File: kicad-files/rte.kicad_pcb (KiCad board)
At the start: 2 copper layers, 120.1 x 58.9 mm, 77 parts, among them J1 APU_LED_INPUT, J10 EXP_GPIO_OUTPUT, J11 OC BUFFER OUTPUT, J12 APU_POWER_SUPPLY_INPUT, J13 APU_POWER_SUPPLY_OUTPUT, J14 RS232, J15 5V_POWER_SUPPLY, J16 UART OUTPUT SELECT, J17 USB_POWER_SUPPLY, J18 EXTERNAL UART, J2 ORANGE_PI_ZERO_SERIAL_OUT, J3 ORANGE_PI_ZERO_CONN2, J4 ORANGE_PI_ZERO_SERIAL_IN, J5 ORANGE_PI_ZERO_CONN1, J6 USB_A1, J7 SPI_OUTPUT, J8 USB_A2, J9 I2C_BUS_OUTPUT, K1 HF3FA, K2 FTR-B3CA003Z, Q1 NDS351AN, Q2 NDS351AN, Q5 Si9435BDY, SW1 RESET, U1 MCP23017, U2 74LS06, U3 MAX3232, U4 74LS06, U5 TXS0104E, U6 MIC5504-1.8YM5, U7 MIC5504-3.3YM5, U8 FDC6331L

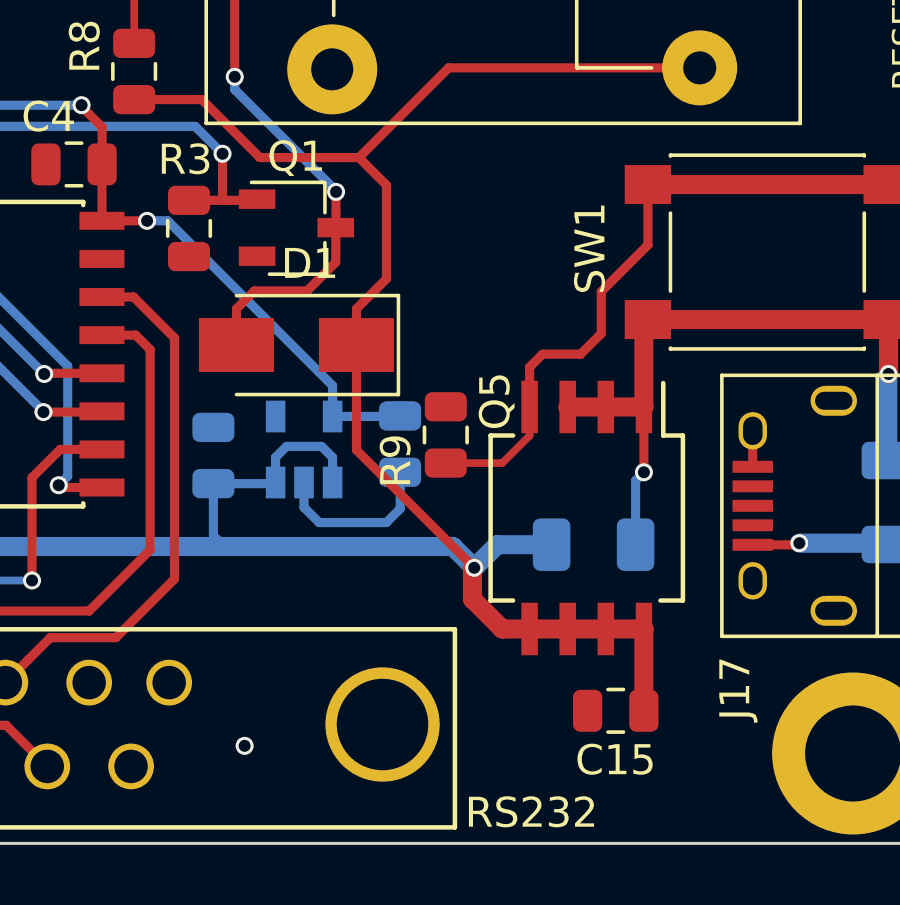
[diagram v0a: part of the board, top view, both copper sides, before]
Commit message: Update Q5 footprint to match the Si9435BDY recommended footprint
Signed-off-by: Michał Żygowski <michal.zygowski@3mdeb.com>
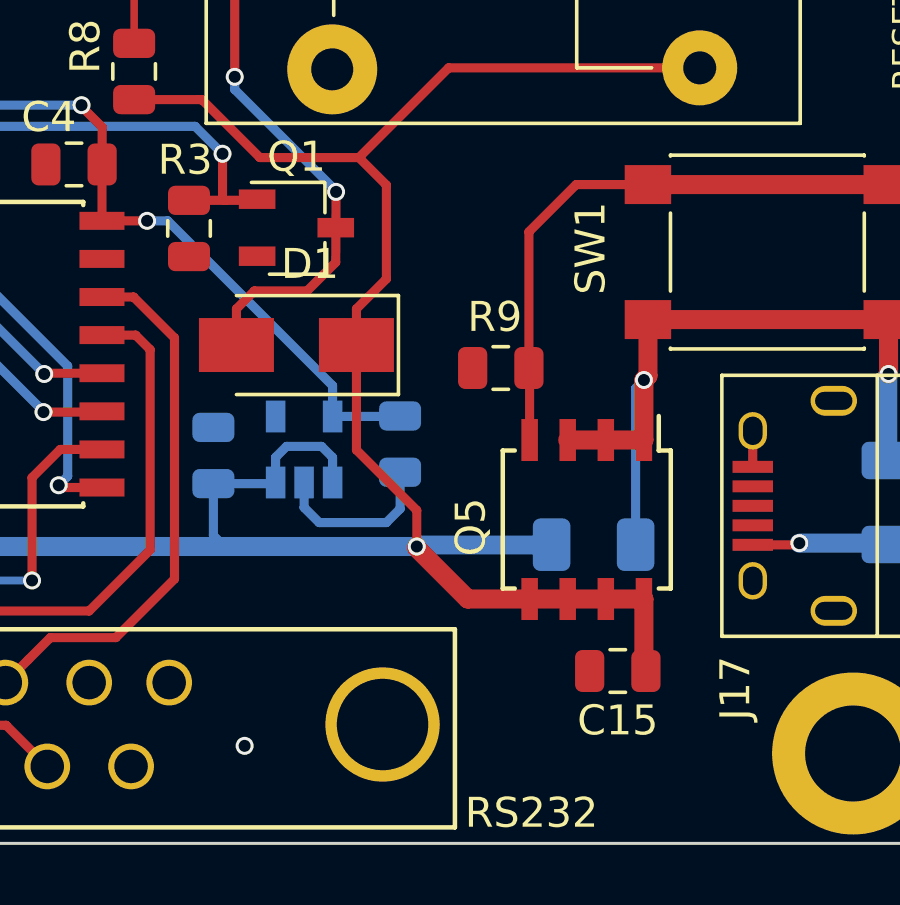
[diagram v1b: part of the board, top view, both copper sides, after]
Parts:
- moved R9 2.89 mm to (196.6, 110.9), turned to 0 degrees
- moved C15 1.33 mm to (200.5, 121.0)
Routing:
- net Net-(Q5-Pad4): track 21.9 -> 19.5 mm
- net Net-(F1-Pad1): track 22.9 -> 25.2 mm
- net +5V: track 240.8 -> 239.6 mm
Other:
- net class Default removed
- net class Power removed
- net class Thin removed

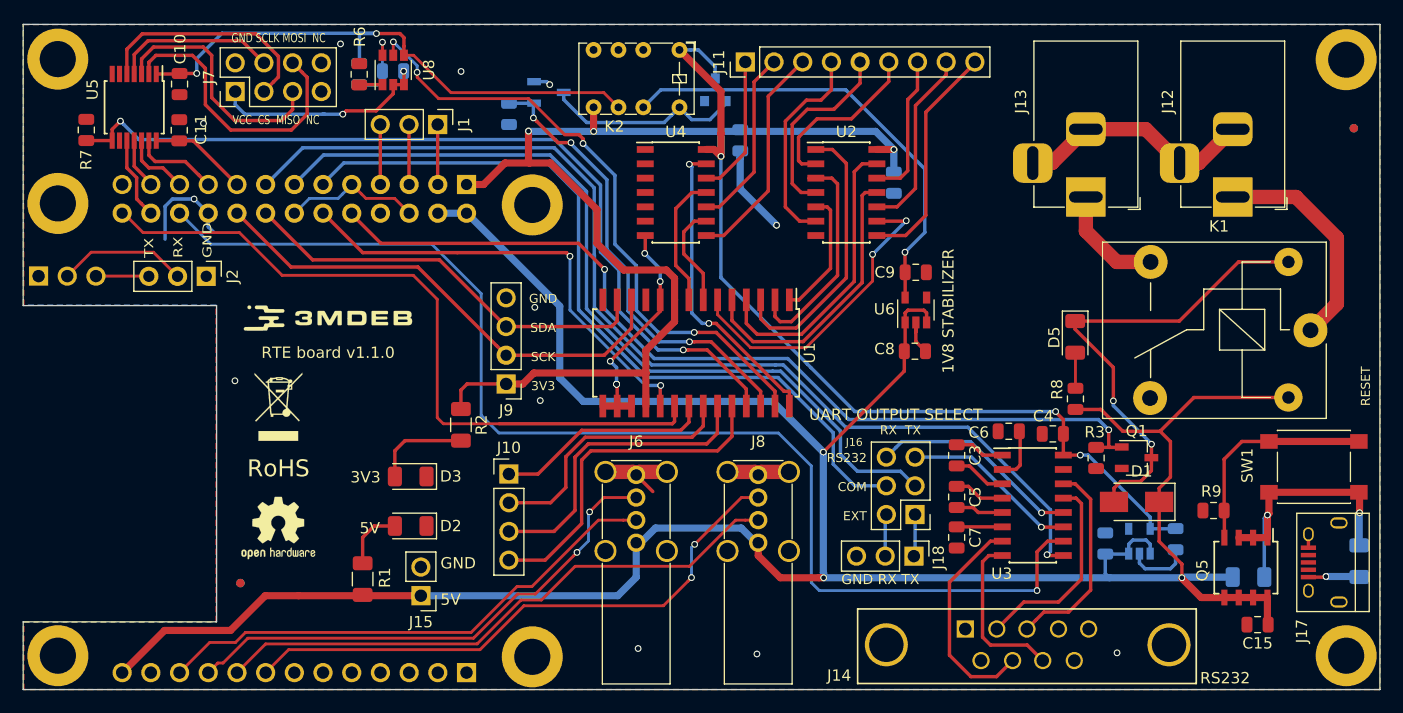
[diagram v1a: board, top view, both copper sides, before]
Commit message: Refactor USB data lines to be more equal in length
Signed-off-by: Michał Żygowski <michal.zygowski@3mdeb.com>
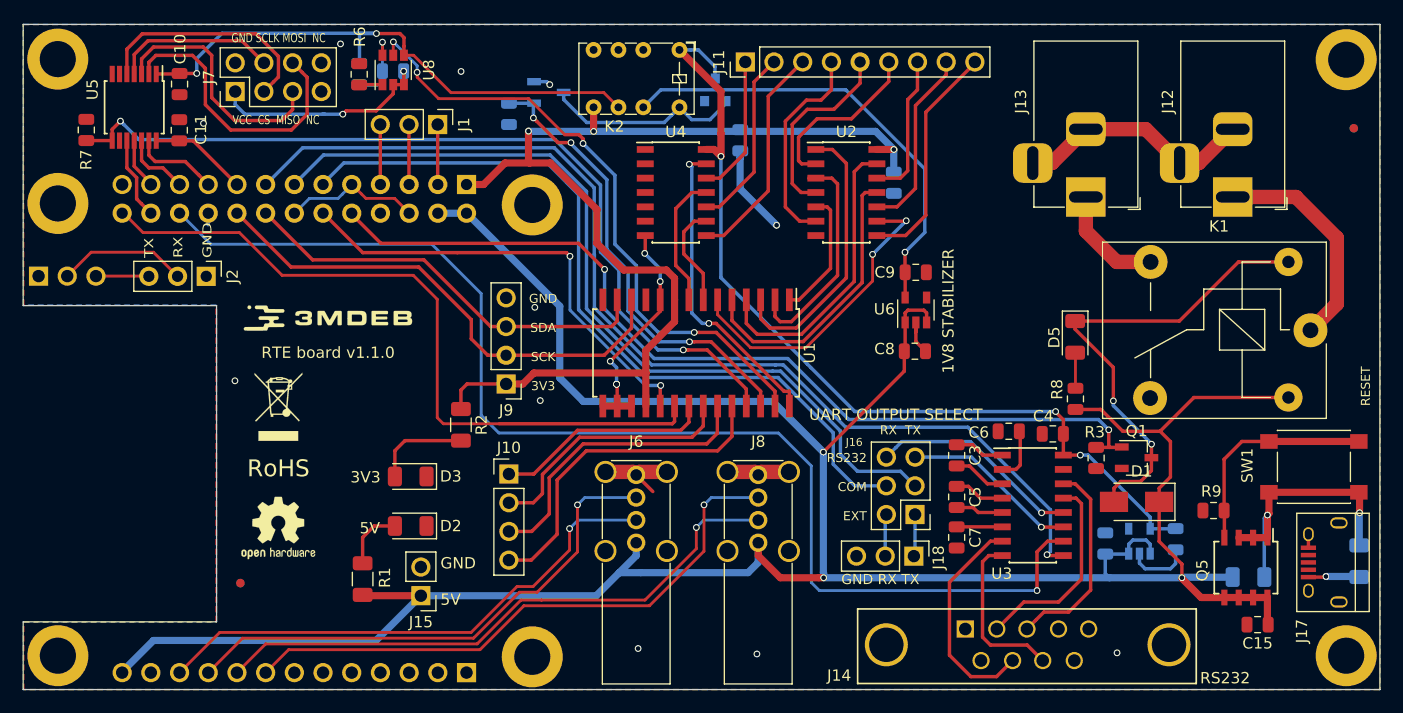
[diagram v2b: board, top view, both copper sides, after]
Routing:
- net GND: track 76.3 -> 68.0 mm, vias 17 -> 16
- net +5V: track 239.6 -> 246.3 mm
- net /USB_D2-: track 46.0 -> 47.1 mm, vias 0 -> 1
- net /USB_D3-: track 51.8 -> 52.9 mm, vias 0 -> 1
- net /TWI1_SCK: track 43.6 -> 44.6 mm
- net /USB_D2+: track 45.9 -> 46.9 mm, vias 2 -> 1
- net /E_GPA2: track 27.2 -> 26.3 mm
- net /USB_D3+: track 51.7 -> 52.5 mm, vias 2 -> 1
- net /E_GPA1: track 23.4 -> 22.8 mm

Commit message: kicad-files/rte.kicad_pcb: Change board version to v1.1.1
Signed-off-by: Michał Żygowski <michal.zygowski@3mdeb.com>
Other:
- board text added: "RTE board v1.1.1"
- board text removed: "RTE board v1.1.0"
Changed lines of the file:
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@@
 		)
 	)
-	(gr_text "RTE board v1.1.0"
+	(gr_text "RTE board v1.1.1"
 		(at 118.2243 96.9264 0)
 		(layer "F.SilkS")
